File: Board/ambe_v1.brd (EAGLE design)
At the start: 48.9 x 52.1 mm, 33 parts, among them IC3 AMBE-3000LQFP-128

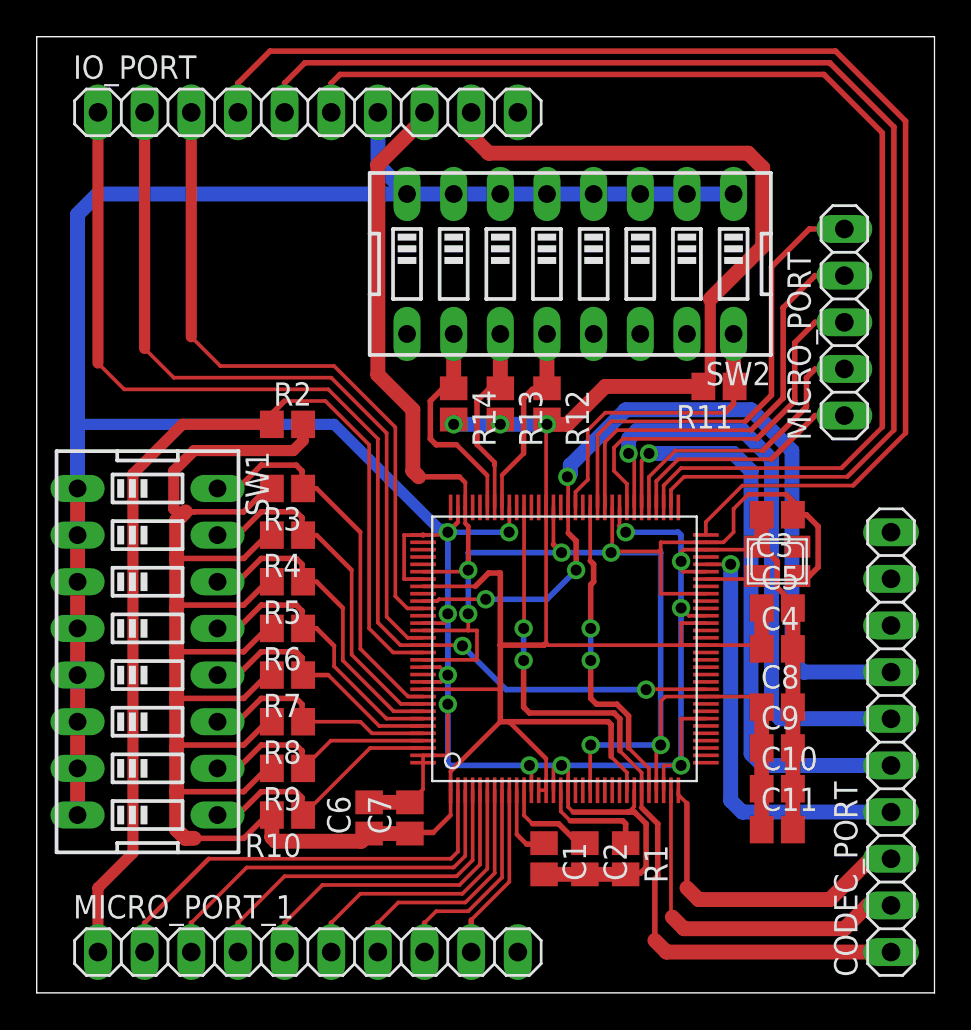
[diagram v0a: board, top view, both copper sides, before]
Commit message: Reposition vias on board
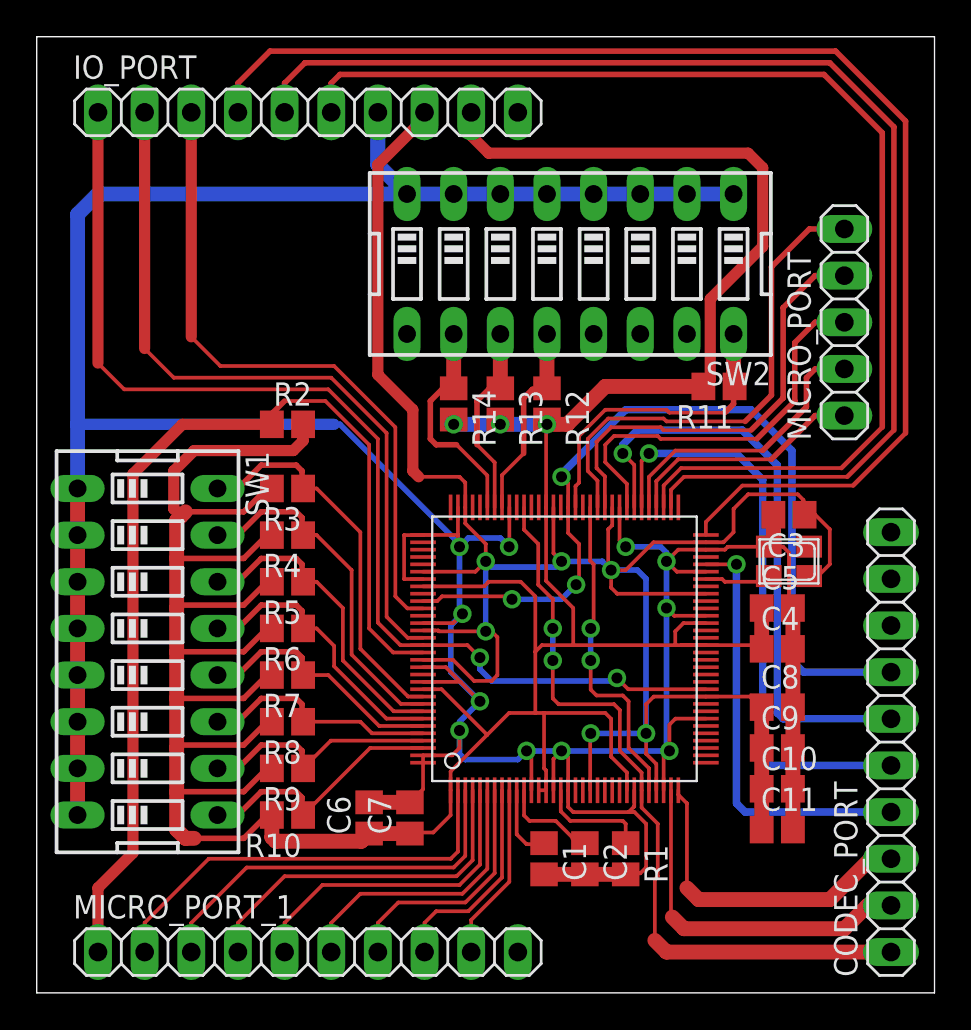
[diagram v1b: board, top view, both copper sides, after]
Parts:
- moved C3 0.64 mm to (41.0, 26.0)
- moved Q1 0.64 mm to (41.0, 23.5)
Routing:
- net GND: track 218.0 -> 224.3 mm
- net 1V8: track 116.5 -> 121.6 mm
- net CODEC_FSN: track 46.3 -> 47.3 mm
- net CODEC_CLKN: track 42.5 -> 41.5 mm
- net RXRQST: track 20.8 -> 21.7 mm
- net RXRDY: track 23.2 -> 24.0 mm
- net X1: track 2.86 -> 3.61 mm
- net TXFRM: track 26.1 -> 26.9 mm
